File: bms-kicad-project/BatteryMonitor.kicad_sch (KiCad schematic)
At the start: 1 part

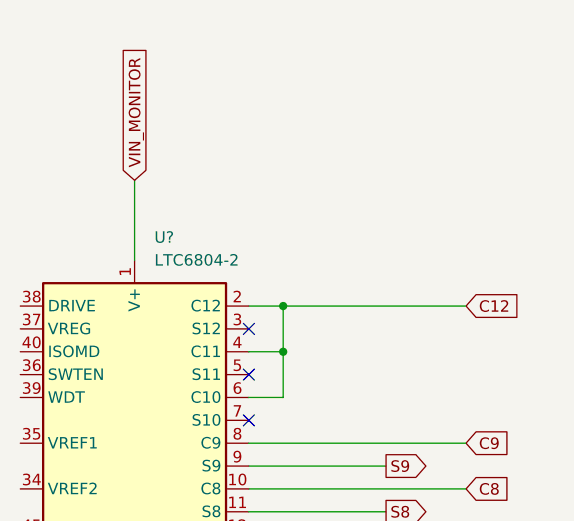
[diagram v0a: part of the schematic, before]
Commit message: feat: update bms references
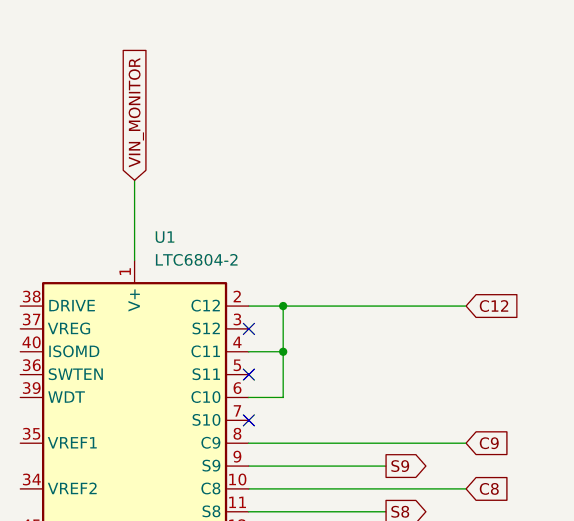
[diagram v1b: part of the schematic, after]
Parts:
- gave numbers to parts that had none: 1
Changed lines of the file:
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@@
   (symbol (lib_id "FixedWing:LTC6804-2") (at 193.04 127 0) (unit 1)
     (in_bom yes) (on_board yes) (dnp no) (fields_autoplaced)
-    (property "Reference" "U?" (at 195.2341 88.9 0)
+    (property "Reference" "U1" (at 195.2341 88.9 0)
       (effects (font (size 1.27 1.27)) (justify left))
     )
@@
       (project "bms-board"
         (path "/8a7831d1-a913-4f04-8780-225d2234b41d/1e9f81b4-c330-4dde-84b6-9168ce482c70"
-          (reference "U?") (unit 1)
+          (reference "U1") (unit 1)
         )
       )

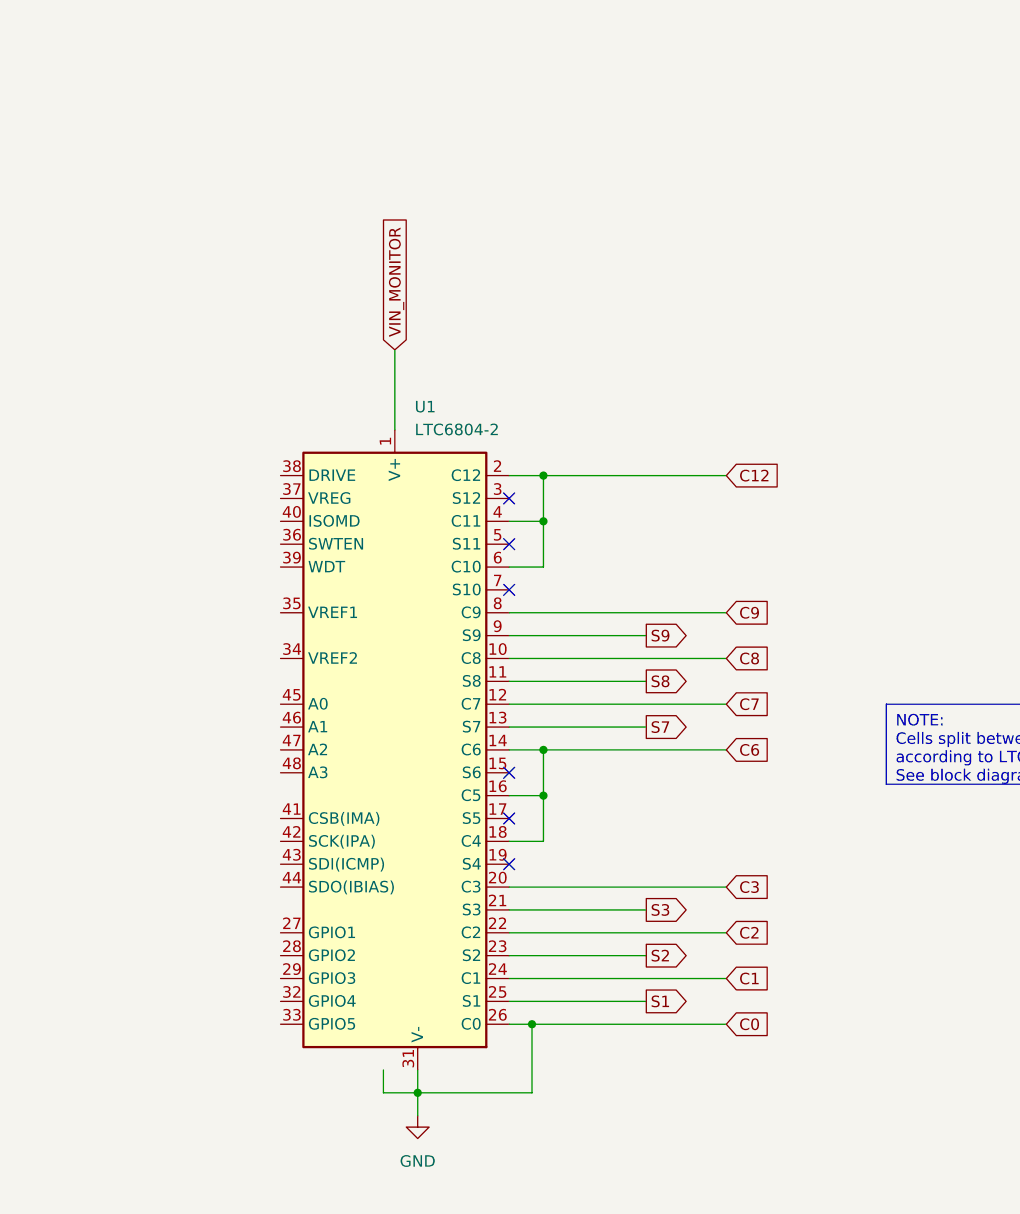
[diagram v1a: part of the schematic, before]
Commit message: Feature: Add RP2040 MCU, folder for 3D models of components, continuing edits on other schematics (#15)
* hierarchical label conversion and readability changes

* feat: added minimal MCU schematic, 3D component model folder

* feat:continuing work on integrating RP2040 MCU

* feat: Added 3D models for connector and Flash ROM

* Added 3D Models in Cell Filtering and Balancing Sch.

* feat. Added most 3D models for footprints

* feat: continuing work on MCU circuit

* feat: finished preliminary RP2040 schematic design

---------

Co-authored-by: Dhruv Dingari <dingari.d@northeastern.edu>
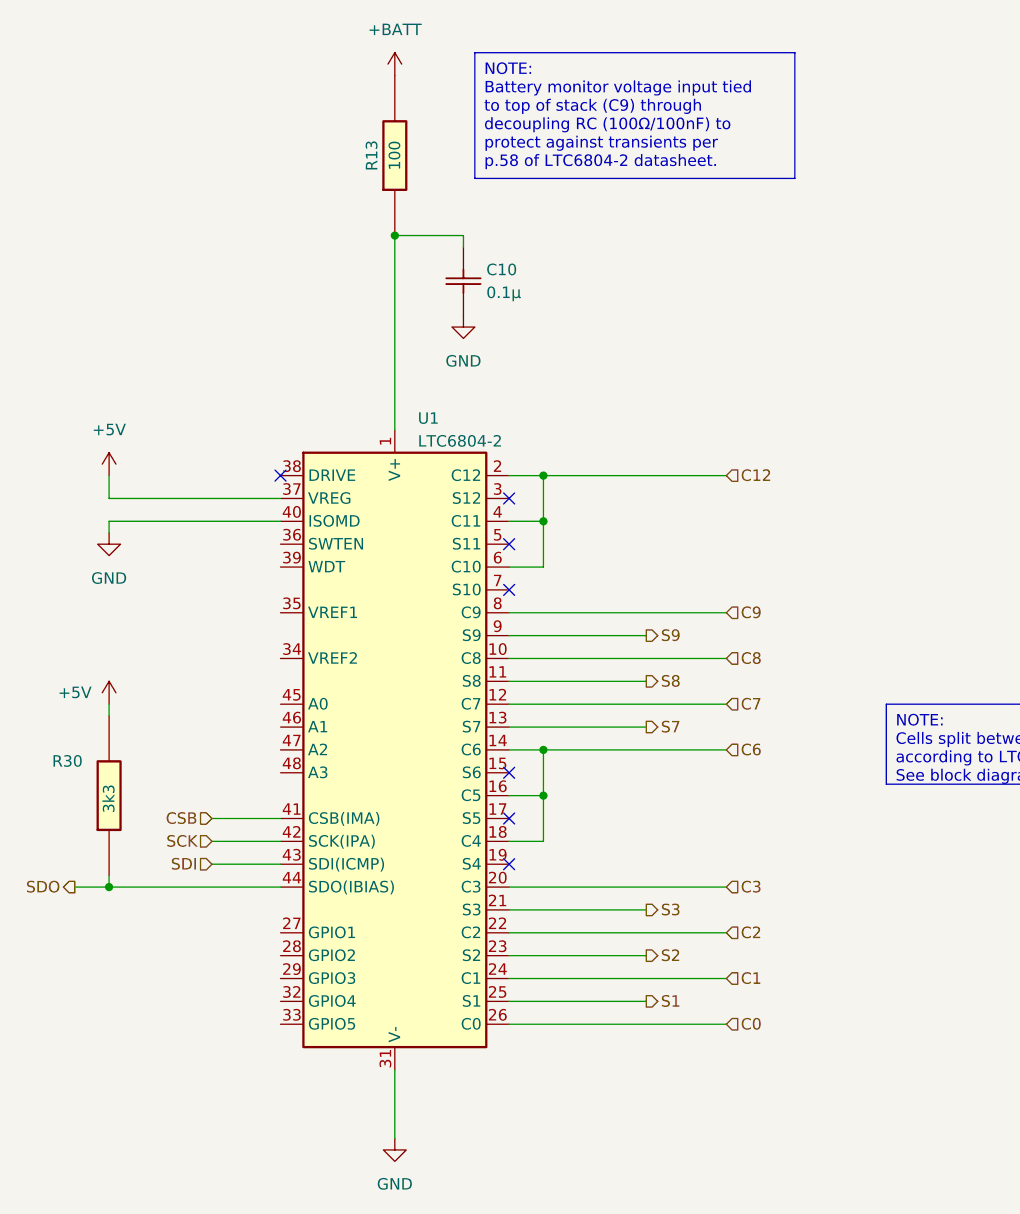
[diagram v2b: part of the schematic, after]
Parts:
- added C10: 0.1µ, FixedWing:CAP_GCJ-18_MUR, symbol FixedWing:GCJ188R72A104KA01D
- added R13: 100, RESC2012X50N, symbol FixedWing:CRCW0805100RFKEA
- added R30: 3k3, RESC2012X50N, symbol FixedWing:CRCW08053K30JNEA
- U1: footprint Package_SO:SSOP-48_5.3x12.8mm_P0.5mm -> FixedWing:SSOP-48_5.3x12.8mm_P0.5mm
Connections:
- net GND: now also U1.40 (ISOMD), C10.2; no longer U1.26 (C0)
- net +5V: now reaches U1.37 (VREG)
- net +5V: now also R30.2
- net CSB: now reaches U1.41 (CSB(IMA))
- net SCK: now reaches U1.42 (SCK(IPA))
- net SDI: now reaches U1.43 (SDI(ICMP))
- net SDO: now reaches U1.44 (SDO(IBIAS))
- net SDO: now also R30.1
- net VIN_MONITOR: no longer names the net of U1.1 (V+)
- net VIN_MONITOR: now also C10.1, R13.1
- new net +BATT: R13.2
- new net C0: U1.26 (C0)
- no-connect marks 6 -> 7
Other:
- company: (none) -> AeroNU - FixedWing
- title: (none) -> Battery Stack Monitor

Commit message: feat: put filtering and balancing circuits into hierarchical format
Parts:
- renumbered C10 to C2, R30 to R2, R13 to R3
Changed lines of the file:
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@@
   (title_block
     (title "Battery Stack Monitor")
+    (date "2024-08-10")
+    (rev "A")
     (company "AeroNU - FixedWing")
   )
@@
   (symbol (lib_id "FixedWing:CRCW0805100RFKEA") (at 193.04 69.85 90) (unit 1)
     (in_bom yes) (on_board yes) (dnp no)
-    (property "Reference" "R13" (at 190.5 60.96 0)
+    (property "Reference" "R3" (at 190.5 60.96 0)
       (effects (font (size 1.27 1.27)))
     )
@@
       (project "bms-board"
         (path "/8a7831d1-a913-4f04-8780-225d2234b41d/1e9f81b4-c330-4dde-84b6-9168ce482c70"
-          (reference "R13") (unit 1)
+          (reference "R3") (unit 1)
         )
       )
@@
   (symbol (lib_id "power:GND") (at 161.29 102.87 0) (unit 1)
     (in_bom yes) (on_board yes) (dnp no) (fields_autoplaced)
-    (property "Reference" "#PWR036" (at 161.29 109.22 0)
+    (property "Reference" "#PWR04" (at 161.29 109.22 0)
       (effects (font (size 1.27 1.27)) hide)
     )
@@
       (project "bms-board"
         (path "/8a7831d1-a913-4f04-8780-225d2234b41d/1e9f81b4-c330-4dde-84b6-9168ce482c70"
-          (reference "#PWR036") (unit 1)
+          (reference "#PWR04") (unit 1)
         )
       )
@@
   (symbol (lib_id "FixedWing:CRCW08053K30JNEA") (at 161.29 140.97 90) (unit 1)
     (in_bom yes) (on_board yes) (dnp no)
-    (property "Reference" "R30" (at 154.94 128.27 90)
+    (property "Reference" "R2" (at 154.94 128.27 90)
       (effects (font (size 1.27 1.27)) (justify right))
     )
@@
       (project "bms-board"
         (path "/8a7831d1-a913-4f04-8780-225d2234b41d/1e9f81b4-c330-4dde-84b6-9168ce482c70"
-          (reference "R30") (unit 1)
+          (reference "R2") (unit 1)
         )
       )
@@
   (symbol (lib_id "power:+5V") (at 161.29 121.92 0) (unit 1)
     (in_bom yes) (on_board yes) (dnp no)
-    (property "Reference" "#PWR033" (at 161.29 125.73 0)
+    (property "Reference" "#PWR05" (at 161.29 125.73 0)
       (effects (font (size 1.27 1.27)) hide)
     )
@@
       (project "bms-board"
         (path "/8a7831d1-a913-4f04-8780-225d2234b41d/1e9f81b4-c330-4dde-84b6-9168ce482c70"
-          (reference "#PWR033") (unit 1)
+          (reference "#PWR05") (unit 1)
         )
       )
@@
   (symbol (lib_id "power:GND") (at 193.04 170.18 0) (unit 1)
     (in_bom yes) (on_board yes) (dnp no) (fields_autoplaced)
-    (property "Reference" "#PWR04" (at 193.04 176.53 0)
+    (property "Reference" "#PWR07" (at 193.04 176.53 0)
       (effects (font (size 1.27 1.27)) hide)
     )
@@
       (project "bms-board"
         (path "/8a7831d1-a913-4f04-8780-225d2234b41d/1e9f81b4-c330-4dde-84b6-9168ce482c70"
-          (reference "#PWR04") (unit 1)
+          (reference "#PWR07") (unit 1)
         )
       )
@@
   (symbol (lib_id "FixedWing:GCJ188R72A104KA01D") (at 200.66 74.93 180) (unit 1)
     (in_bom yes) (on_board yes) (dnp no)
-    (property "Reference" "C10" (at 203.2 73.66 0)
+    (property "Reference" "C2" (at 203.2 73.66 0)
       (effects (font (size 1.27 1.27)) (justify right))
     )
@@
       (project "bms-board"
         (path "/8a7831d1-a913-4f04-8780-225d2234b41d/1e9f81b4-c330-4dde-84b6-9168ce482c70"
-          (reference "C10") (unit 1)
+          (reference "C2") (unit 1)
         )
       )
@@
   (symbol (lib_id "power:+BATT") (at 193.04 52.07 0) (unit 1)
     (in_bom yes) (on_board yes) (dnp no) (fields_autoplaced)
-    (property "Reference" "#PWR09" (at 193.04 55.88 0)
+    (property "Reference" "#PWR06" (at 193.04 55.88 0)
       (effects (font (size 1.27 1.27)) hide)
     )
@@
       (project "bms-board"
         (path "/8a7831d1-a913-4f04-8780-225d2234b41d/1e9f81b4-c330-4dde-84b6-9168ce482c70"
-          (reference "#PWR09") (unit 1)
-        )
-      )
+          (reference "#PWR06") (unit 1)
+        )
+      )

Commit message: feat: Added comment boxes and fixed 5V Regulator Schematic.
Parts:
- R?: renamed from R2; value 3k3 -> 3.3k
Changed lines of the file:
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@@
   (symbol (lib_id "FixedWing:CRCW08053K30JNEA") (at 161.29 140.97 90) (unit 1)
     (in_bom yes) (on_board yes) (dnp no)
-    (property "Reference" "R2" (at 154.94 128.27 90)
+    (property "Reference" "R?" (at 154.94 128.27 90)
       (effects (font (size 1.27 1.27)) (justify right))
     )
-    (property "Value" "3k3" (at 161.29 130.81 0)
+    (property "Value" "3.3k" (at 161.29 130.81 0)
       (effects (font (size 1.27 1.27)) (justify right))
     )
@@
       (project "bms-board"
         (path "/8a7831d1-a913-4f04-8780-225d2234b41d/1e9f81b4-c330-4dde-84b6-9168ce482c70"
-          (reference "R2") (unit 1)
+          (reference "R?") (unit 1)
         )
       )

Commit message: feat: Added snubber circuit to 5V Regulator schematic
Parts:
- gave numbers to parts that had none: 1
- renumbered C2 to C14, R3 to R51
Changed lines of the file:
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@@
   (symbol (lib_id "FixedWing:CRCW0805100RFKEA") (at 193.04 69.85 90) (unit 1)
     (in_bom yes) (on_board yes) (dnp no)
-    (property "Reference" "R3" (at 190.5 60.96 0)
+    (property "Reference" "R51" (at 190.5 60.96 0)
       (effects (font (size 1.27 1.27)))
     )
@@
       (project "bms-board"
         (path "/8a7831d1-a913-4f04-8780-225d2234b41d/1e9f81b4-c330-4dde-84b6-9168ce482c70"
-          (reference "R3") (unit 1)
+          (reference "R51") (unit 1)
         )
       )
@@
   (symbol (lib_id "FixedWing:CRCW08053K30JNEA") (at 161.29 140.97 90) (unit 1)
     (in_bom yes) (on_board yes) (dnp no)
-    (property "Reference" "R?" (at 154.94 128.27 90)
+    (property "Reference" "R50" (at 154.94 128.27 90)
       (effects (font (size 1.27 1.27)) (justify right))
     )
@@
       (project "bms-board"
         (path "/8a7831d1-a913-4f04-8780-225d2234b41d/1e9f81b4-c330-4dde-84b6-9168ce482c70"
-          (reference "R?") (unit 1)
+          (reference "R50") (unit 1)
         )
       )
@@
   (symbol (lib_id "FixedWing:GCJ188R72A104KA01D") (at 200.66 74.93 180) (unit 1)
     (in_bom yes) (on_board yes) (dnp no)
-    (property "Reference" "C2" (at 203.2 73.66 0)
+    (property "Reference" "C14" (at 203.2 73.66 0)
       (effects (font (size 1.27 1.27)) (justify right))
     )
@@
       (project "bms-board"
         (path "/8a7831d1-a913-4f04-8780-225d2234b41d/1e9f81b4-c330-4dde-84b6-9168ce482c70"
-          (reference "C2") (unit 1)
-        )
-      )
+          (reference "C14") (unit 1)
+        )
+      )

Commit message: feat: added buncha shit, refer to tasks 4 and 8
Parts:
- removed R50: 3.3k, RESC2012X50N, symbol FixedWing:CRCW08053K30JNEA
- added L15: 600Ω, FixedWing:IND_BLM31PG391SN1L_MUR, symbol FixedWing:BLM31PG601SN1L
- added R75: 5.6k, FixedWing:RESC2012X60N, symbol FixedWing:RK73H2ATTD5601F
- renumbered R51 to R76
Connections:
- net +5V: now also R75.2
- net +BATT: now also L15.1; no longer R76.2
- net C12: no longer U1.4 (C11), U1.6 (C10)
- net C6: no longer U1.16 (C5), U1.18 (C4)
- net SDO: now also R75.1
- net S6: now reaches U1.15 (S6)
- net S5: now reaches U1.17 (S5)
- net S4: now reaches U1.19 (S4)
- net S12: now reaches U1.3 (S12)
- net S11: now reaches U1.5 (S11)
- net S10: now reaches U1.7 (S10)
- new net: L15.2, R76.2
- new net C10: U1.6 (C10)
- new net C11: U1.4 (C11)
- new net C4: U1.18 (C4)
- new net C5: U1.16 (C5)
- no-connect marks 7 -> 1
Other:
- moved on the sheet: R76
